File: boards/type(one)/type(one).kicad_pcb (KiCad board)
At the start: 2 copper layers, 101.6 x 127 mm, 37 parts, among them J1 IDC-Header_02x03, J2 IDC-Header_02x05, J3 Conn_01x02, J4 Conn_01x05, J5 Conn_01x05, J6 Conn_01x03, J7 Conn_01x02, Q1 2N2907, Q2 2n2222, Q3 IRF4905, Q4 2n2222, U1 ESP32-WROOM-UE, U2 LM393, U4 LM1117T-5.0, U5 LM1117T-3.3

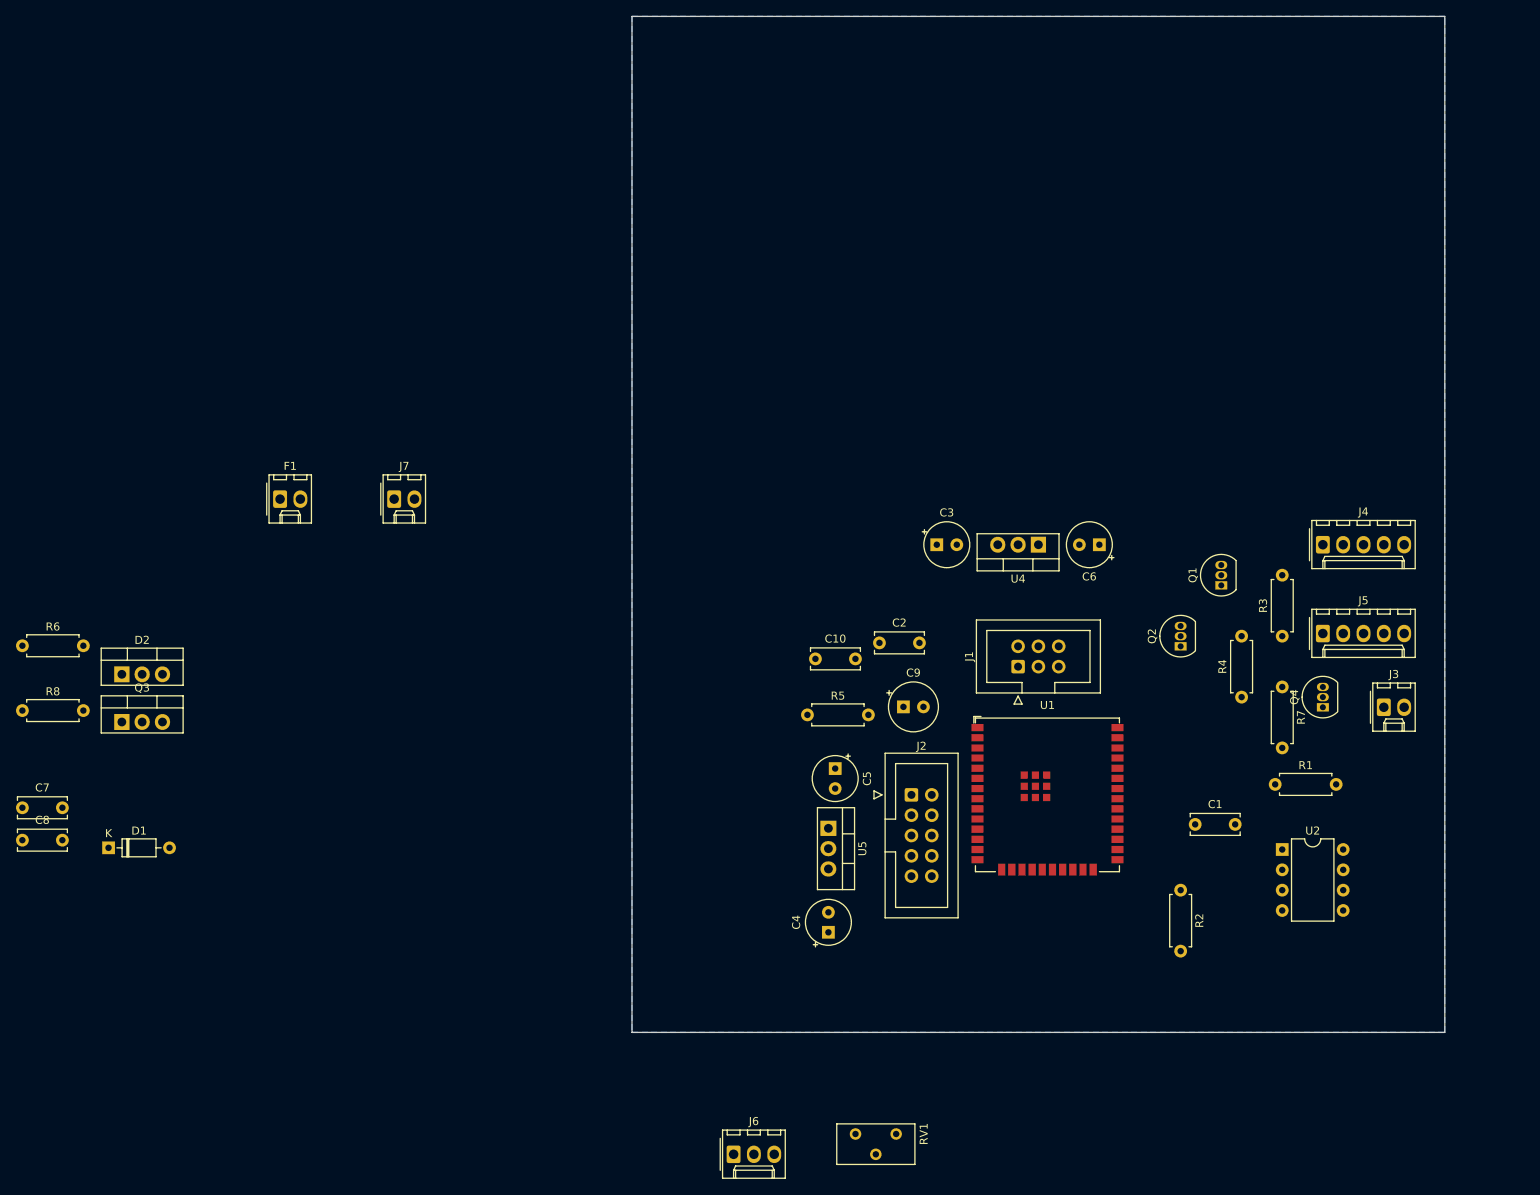
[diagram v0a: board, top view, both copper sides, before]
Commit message: create pcb and update circuit
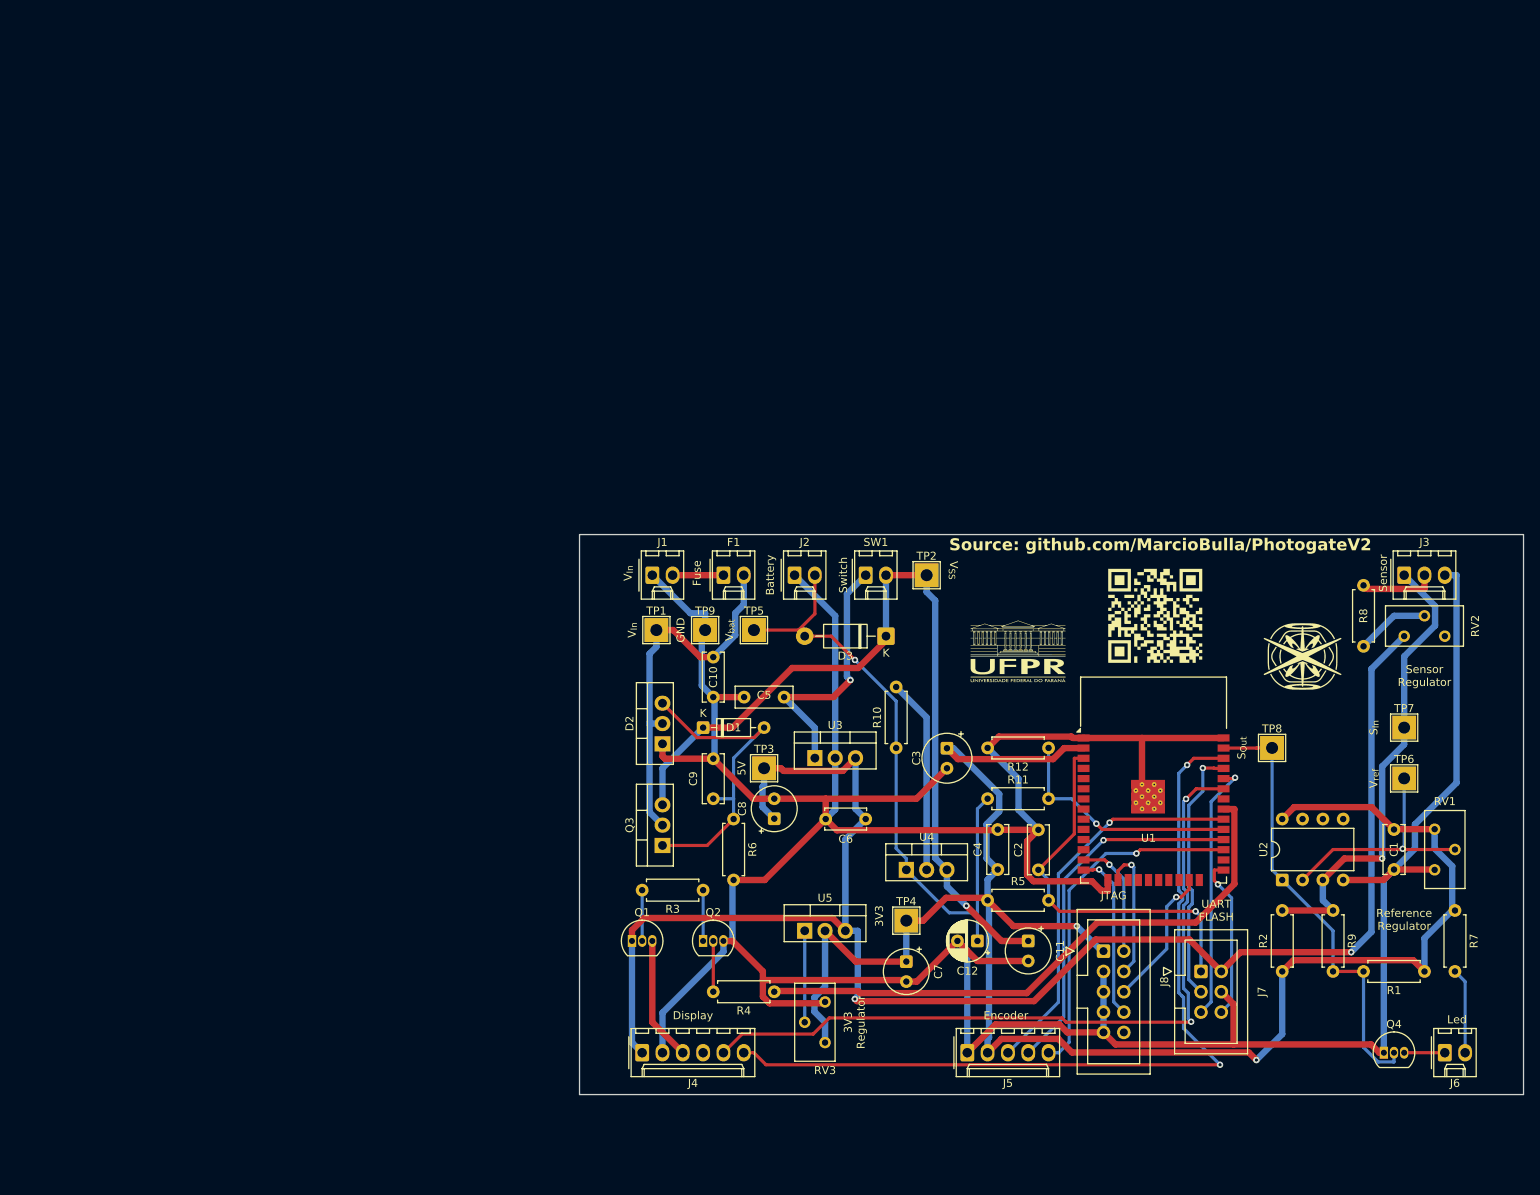
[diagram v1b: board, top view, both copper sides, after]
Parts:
- added C11: 10uF, Capacitor_THT:CP_Radial_Tantal_D5.5mm_P2.50mm, F.Cu at (151.1, 115.6)
- added C12: 100uF, Capacitor_THT:CP_Radial_D5.0mm_P2.50mm, F.Cu at (144.8, 115.6)
- added D3: 1N4001, Diode_THT:D_DO-41_SOD81_P10.16mm_Horizontal, F.Cu at (133.3, 77.5)
- added J8: Conn_02x05_Odd_Even, Connector_IDC:IDC-Header_2x05_P2.54mm_Vertical, F.Cu at (160.5, 116.8)
- added QRcode git: LOGO, LOGO, F.Cu at (167.0, 74.9)
- added R10: 12, Resistor_THT:R_Axial_DIN0207_L6.3mm_D2.5mm_P7.62mm_Horizontal, F.Cu at (134.6, 91.4)
- added R11: 20k, Resistor_THT:R_Axial_DIN0207_L6.3mm_D2.5mm_P7.62mm_Horizontal, F.Cu at (146.1, 97.8)
- added R12: 6k8, Resistor_THT:R_Axial_DIN0207_L6.3mm_D2.5mm_P7.62mm_Horizontal, F.Cu at (153.7, 91.4)
- added R9: 50k, Resistor_THT:R_Axial_DIN0207_L6.3mm_D2.5mm_P7.62mm_Horizontal, F.Cu at (189.2, 111.8)
- added RV2: 1k, Potentiometer_THT:Potentiometer_Bourns_3386X_Horizontal, F.Cu at (198.1, 77.5)
- added RV3: 1k, Potentiometer_THT:Potentiometer_Bourns_3386X_Horizontal, F.Cu at (125.7, 128.3)
- added SW1: Switch, Connector_Molex:Molex_KK-254_AE-6410-02A_1x02_P2.54mm_Vertical, F.Cu at (130.8, 69.8)
- added TP1: TestPoint_Probe, TestPoint:TestPoint_THTPad_3.0x3.0mm_Drill1.5mm, F.Cu at (104.6, 76.7)
- added TP2: TestPoint_Probe, TestPoint:TestPoint_THTPad_3.0x3.0mm_Drill1.5mm, F.Cu at (138.4, 69.8)
- added TP3: TestPoint_Probe, TestPoint:TestPoint_THTPad_3.0x3.0mm_Drill1.5mm, F.Cu at (118.1, 94.0)
- added TP4: TestPoint_Probe, TestPoint:TestPoint_THTPad_3.0x3.0mm_Drill1.5mm, F.Cu at (135.9, 113.0)
- added TP5: TestPoint_Probe, TestPoint:TestPoint_THTPad_3.0x3.0mm_Drill1.5mm, F.Cu at (116.8, 76.7)
- added TP6: TestPoint_Probe, TestPoint:TestPoint_THTPad_3.0x3.0mm_Drill1.5mm, F.Cu at (198.1, 95.2)
- added TP7: TestPoint_Probe, TestPoint:TestPoint_THTPad_3.0x3.0mm_Drill1.5mm, F.Cu at (198.1, 88.9)
- added TP8: TestPoint_Probe, TestPoint:TestPoint_THTPad_3.0x3.0mm_Drill1.5mm, F.Cu at (181.6, 91.4)
- added TP9: TestPoint_Probe, TestPoint:TestPoint_THTPad_3.0x3.0mm_Drill1.5mm, F.Cu at (110.7, 76.7)
- added U3: LM7805_TO220, Package_TO_SOT_THT:TO-220-3_Vertical, F.Cu at (124.5, 92.7)
- added logo1: UFPR, LOGO, F.Cu at (149.9, 79.4)
- added logo2: Lorxi, LOGO, F.Cu at (185.4, 80.0)
- C3: value 10uF -> 22uF; footprint Capacitor_THT:CP_Radial_Tantal_D5.5mm_P2.50mm -> Capacitor_THT:CP_Radial_Tantal_D6.0mm_P2.50mm
- C4: value 10uF -> 100nF; footprint Capacitor_THT:CP_Radial_Tantal_D5.5mm_P2.50mm -> Capacitor_THT:C_Disc_D6.0mm_W2.5mm_P5.00mm
- C5: value 10uF -> 220nF; footprint Capacitor_THT:CP_Radial_Tantal_D5.5mm_P2.50mm -> Capacitor_THT:C_Rect_L7.0mm_W2.5mm_P5.00mm
- C6: value 10uF -> 100nF; footprint Capacitor_THT:CP_Radial_Tantal_D5.5mm_P2.50mm -> Capacitor_THT:C_Disc_D5.0mm_W2.5mm_P5.00mm
- C7: value 100nF -> 100uF; footprint Capacitor_THT:C_Disc_D6.0mm_W2.5mm_P5.00mm -> Capacitor_THT:CP_Radial_Tantal_D5.5mm_P2.50mm
- C8: value 100nF -> 10uF; footprint Capacitor_THT:C_Disc_D6.0mm_W2.5mm_P5.00mm -> Capacitor_THT:CP_Radial_Tantal_D5.5mm_P2.50mm
- C9: value 22uF -> 100nF; footprint Capacitor_THT:CP_Radial_Tantal_D6.0mm_P2.50mm -> Capacitor_THT:C_Disc_D6.0mm_W2.5mm_P5.00mm
- F1: value 1A -> 300mA
- J1: value IDC-Header_02x03 -> Conn_01x02; footprint Connector_IDC:IDC-Header_2x03_P2.54mm_Vertical -> Connector_Molex:Molex_KK-254_AE-6410-02A_1x02_P2.54mm_Vertical
- J2: value IDC-Header_02x05 -> Conn_01x02; footprint Connector_IDC:IDC-Header_2x05_P2.54mm_Vertical -> Connector_Molex:Molex_KK-254_AE-6410-02A_1x02_P2.54mm_Vertical
- J3: value Conn_01x02 -> Conn_01x03; footprint Connector_Molex:Molex_KK-254_AE-6410-02A_1x02_P2.54mm_Vertical -> Connector_Molex:Molex_KK-254_AE-6410-03A_1x03_P2.54mm_Vertical
- J4: value Conn_01x05 -> Conn_01x06; footprint Connector_Molex:Molex_KK-254_AE-6410-05A_1x05_P2.54mm_Vertical -> Connector_Molex:Molex_KK-254_AE-6410-06A_1x06_P2.54mm_Vertical
- J6: value Conn_01x03 -> Conn_01x02; footprint Connector_Molex:Molex_KK-254_AE-6410-03A_1x03_P2.54mm_Vertical -> Connector_Molex:Molex_KK-254_AE-6410-02A_1x02_P2.54mm_Vertical
- J7: value Conn_01x02 -> Conn_02x03_Odd_Even; footprint Connector_Molex:Molex_KK-254_AE-6410-02A_1x02_P2.54mm_Vertical -> Connector_IDC:IDC-Header_2x03_P2.54mm_Vertical
- Q4: value 2n2222 -> 2N7000
- R3, R4: value R_US -> 1k
- R7: value 150 -> 10k
- U1: value ESP32-WROOM-UE -> ESP32-WROOM-32U; footprint PCM_Espressif:ESP32-WROOM-32UE -> RF_Module:ESP32-WROOM-32
- U4: value LM1117T-5.0 -> LM1117DT-ADJ
- U5: value LM1117T-3.3 -> LM1117DT-ADJ
- moved R8 168.4 mm to (193.0, 71.1), turned to -90 degrees
- moved J7 116.9 mm to (172.7, 119.4)
- moved C7 112.2 mm to (135.9, 118.2), turned to -90 degrees
- moved J4 106.2 mm to (102.9, 129.5)
- moved C8 94.0 mm to (119.4, 100.3), turned to 90 degrees
- moved R6 91.5 mm to (114.3, 100.3), turned to -90 degrees
- moved J6 89.8 mm to (203.2, 129.5)
- moved Q1 86.0 mm to (101.6, 115.6), turned to 0 degrees
- moved R3 79.0 mm to (110.5, 109.2), turned to 180 degrees
- moved RV1 77.3 mm to (201.9, 101.6), turned to 0 degrees
- moved D1 75.8 mm to (110.5, 88.9)
- moved Q2 70.1 mm to (110.5, 115.6), turned to 0 degrees
- moved Q3 69.3 mm to (105.4, 103.6), turned to 90 degrees
- moved R4 69.1 mm to (119.4, 121.9), turned to 180 degrees
- moved J5 68.7 mm to (143.5, 129.5)
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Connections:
- C1 pad 1: /SENSOR -> +3V3
- C10 pad 1: +3V3 -> Net-(D2-A)
- C3 pad 1: Net-(D1-K) -> +3V3
- C4 pad 1: Net-(D1-K) -> +3V3
- C5 pad 1: +3V3 -> VDC
- C7 pad 1: Net-(D1-A) -> +3V3
- C8 pad 1: Net-(D2-A) -> +5V
- C9 pad 1: +3V3 -> Net-(D1-A)
- D1 pad 1: Net-(D1-K) -> VSS
- F1 pad 1: VDC -> VDD
- J1 pad 1: /EN -> GND
- J1 pad 2: +5V -> VDD
- J2 pad 1: +3.3V -> GND
- J2 pad 2: /TMS -> Net-(D3-A)
- J3 pad 1: Net-(J3-Pin_1) -> /PH_K
- J4 pad 3: /SDA -> /PWM_5V
- J4 pad 4: /SCL -> unconnected-(J4-Pin_4-Pad4)
- J4 pad 5: /PWM_5V -> /SDA
- J6 pad 1: /PH_K -> Net-(J6-Pin_1)
- J7 pad 1: GND -> /EN
- J7 pad 2: VDC -> +5V
- Q2 pad 1: GND -> Net-(Q2-C)
- Q2 pad 3: Net-(Q2-C) -> GND
- Q3 pad 1: Net-(D2-A) -> Net-(D1-A)
- Q3 pad 2: Net-(D1-A) -> Net-(D2-A)
- Q3 pad 3: Net-(D1-K) -> VSS
- Q4 pad 3: Net-(J3-Pin_1) -> Net-(J6-Pin_1)
- R2 pad 1: /PH_K -> +3V3
- R2 pad 2: GND -> /PH_K
- R7 pad 2: Net-(J3-Pin_2) -> Net-(J6-Pin_2)
- R8 pad 1: Net-(J6-Pin_2) -> Net-(J3-Pin_2)
- R8 pad 2: +5V -> Net-(R8-Pad2)
- RV1 pad 2: Net-(U2A-+) -> Net-(U2A--)
- U1 pad 17: (no net) -> unconnected-(U1-SHD/SD2-Pad17)
- U1 pad 18: (no net) -> unconnected-(U1-SWP/SD3-Pad18)
- U1 pad 19: (no net) -> unconnected-(U1-SCS/CMD-Pad19)
- U1 pad 20: (no net) -> unconnected-(U1-SCK/CLK-Pad20)
- U1 pad 21: (no net) -> unconnected-(U1-SDO/SD0-Pad21)
- U1 pad 22: (no net) -> unconnected-(U1-SDI/SD1-Pad22)
- U1 pad 27: /DT -> /CLK
- U1 pad 28: /SW -> /DT
- U1 pad 29: /CLK -> /V_bat
- U1 pad 30: /SENSOR -> /SW
- U1 pad 32: (no net) -> unconnected-(U1-NC-Pad32)
- U1 pad 37: unconnected-(U1-GPIO23-Pad37) -> /SENSOR
- U1 pad 39: unconnected-(U1-GND_THERMAL-Pad39) -> GND
- U2 pad 2: /PH_K -> Net-(U2A--)
- U2 pad 3: Net-(U2A-+) -> /PH_K
- U2 pad 5: (no net) -> unconnected-(U2B-+-Pad5)
- U2 pad 6: (no net) -> unconnected-(U2B---Pad6)
- U2 pad 7: (no net) -> unconnected-(U2-Pad7)
- U4 pad 1: GND -> Net-(D3-A)
- U4 pad 2: +5V -> +8V4
- U4 pad 3: Net-(D1-K) -> VSS
- U5 pad 1: GND -> Net-(U5-ADJ)
- U5 pad 3: Net-(D1-K) -> +5V
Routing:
- net GND: track 0.00 -> 480.3 mm
- net +3V3: track 0.00 -> 230.0 mm, vias 0 -> 2
- net +5V: track 0.00 -> 206.7 mm, vias 0 -> 2
- net /SCL: track 0.00 -> 105.9 mm, vias 0 -> 2
- net VSS: track 0.00 -> 105.3 mm, vias 0 -> 1
- net /SDA: track 0.00 -> 94.5 mm, vias 0 -> 2
- net Net-(D3-A): track 0.00 -> 80.2 mm, vias 0 -> 1
- net /PWM_3V3: track 0.00 -> 74.0 mm
- net /PH_K: track 0.00 -> 59.0 mm, vias 0 -> 1
- net /SENSOR: track 0.00 -> 56.2 mm
- net /SW: track 0.00 -> 48.4 mm, vias 0 -> 1
- net /EN: track 0.00 -> 48.0 mm, vias 0 -> 1
- net Net-(D2-A): track 0.00 -> 47.4 mm
- net /DT: track 0.00 -> 45.5 mm, vias 0 -> 1
- net /CLK: track 0.00 -> 43.5 mm, vias 0 -> 1
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- removed copper zone on B.Cu, net GND
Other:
- board size 101.6 x 127 mm -> 118 x 70 mm
- board text added: "3V3"
- board text added: "3V3 Regulator"
- board text added: "5V"
- board text added: "Battery"
- board text added: "Display"
- board text added: "EN"
- board text added: "Encoder"
- board text added: "Fuse"
- board text added: "GND"
- board text added: "IO0"
- board text added: "JTAG"
- board text added: "Led"
- board text added: "NC"
- board text added: "RX"
- board text added: "Reference Regulator"
- board text added: "S_{In}"
- board text added: "S_{Out}"
- board text added: "Sensor"
- board text added: "Sensor Regulator"
- board text added: "Source: github.com/MarcioBulla/PhotogateV2"
- board text added: "Switch"
- board text added: "TCK"
- board text added: "TDI"
- board text added: "TDO"
- board text added: "TMS"
- board text added: "TX"
- board text added: "UART FLASH"
- board text added: "V_{In}"
- board text added: "V_{SS}"
- board text added: "V_{bat}"
- board text added: "V_{ref}"
